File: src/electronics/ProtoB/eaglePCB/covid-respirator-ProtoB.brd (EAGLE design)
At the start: 160 x 100 mm, 18 parts, among them IC2 L7805CV-DG, Q1 VNP35N07-E, T2 BC548

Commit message: update protoB schematic
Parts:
- removed F1: 8A, fuse:19560
- removed Q1: VNP35N07-E, transistor-fet:TO220
- added IC1: (no value), analog-devices:SO8
- added IC3, IC4: AD8607R, analog-devices:SO8
- added LCD1: LCD_2X16_SIL, lcd_2x16_led_backlight:HY-1602F
- added LED1, LED3: ROUGE, led:LED3MM
- added LED2: VERTE, led:LED3MM
- added R10: 680, rcl:0207/10
- added R11: 10k, pot:SM-42/43B
- added R12: 68k, rcl:0207/10
- added R13: 33k, rcl:0207/10
- added R14: 22k, rcl:0207/10
- added R15: 12k, rcl:0207/10
- added R16, R17: 8.2k, rcl:0207/10
- added R18: 5.6k, rcl:0207/10
- added R19: 3.3k, rcl:0207/10
- added R20: 2.2k, rcl:0207/10
- added R21, R22, R26: 270, rcl:0207/10
- added R23, R24, R25: 10k, rcl:0207/10
- added R9: 150, rcl:0207/10
- added S1, S2, S3, S4, S5, S6, S7, S8: TL32YO, switch:TL3XYO
- C2: value 47uF/25v -> 10uF/25v
- C4: value 10uF -> 100nF
- R1, R4: value 100 -> 1.5k
- R2: value 3k -> 4k7
- R6: value 1k -> 12k
- R7: value 1k -> 1.5k
- R8: value 1k -> 150
- moved R4 137.2 mm to (-71.1, -88.9)
- moved R1 127.0 mm to (-71.1, -83.8)
- moved R8 95.7 mm to (-71.1, -133.3)
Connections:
- net A3 renamed A2
- removed net D6: R4.2
- new net +5VNUCLEO: IC3.4, LCD1.2, R1.1, R11.3, R16.1, R8.1
- new net 6546876: C4.1, IC1.3, R5.1
- new net A0: R12.2, R13.2, R14.2, R15.2, R16.2, R17.2, R18.2, R19.2, R20.2
- new net D10: LCD1.12
- new net D11: LCD1.13
- new net D12: LCD1.14
- new net D2: IC3.3, R24.1
- new net D4: IC3.5, R23.1
- new net D7: LCD1.4
- new net D8: LCD1.6
- new net D9: LCD1.11
- new net N$10: LCD1.3, R11.2
- new net N$11: R12.1, S8.1
- new net N$14: R13.1, S7.1
- new net N$15: R14.1, S6.1
- new net N$16: R15.1, S5.1
- new net N$18: R17.1, S4.1
- new net N$19: R18.1, S3.1
- new net N$20: R19.1, S2.1
- new net N$21: R20.1, S1.1
- new net N$22: LED3.K, R26.1
- new net N$23: LED1.K, R21.1
- new net N$24: LED2.K, R22.1
- new net N$26: LED3.A
- new net N$7: LCD1.15, R8.2
- new net N$8: IC1.2, IC1.6, R9.2
- new net PB13: LED2.A
- new net PC4: LED1.A
- new net V+: IC4.8
- new net V-: IC4.4
- net +12V: no longer F1.2
- net A1: now also R10.1, R9.1; no longer C4.1, R5.1
- net AGND: now also IC1.4, R10.2
- net AREF: now also IC1.7
- net D5: now also IC4.3, R25.1; no longer R1.2
- net GND: now also IC3.8, LCD1.1, LCD1.16, LCD1.5, R11.1, R21.2, R22.2, R23.2, R24.2, R25.2, R26.2, R4.2, S1.2, S2.2, S3.2, S4.2, S5.2, S6.2, S7.2, S8.2; no longer Q1.3, R8.1
- net N$1: now also IC4.1; no longer R1.1
- net N$4: now also IC3.2, IC3.6, IC4.2, R1.2, R4.1; no longer Q1.2
- net N$5: now also IC3.1; no longer F1.1
- net N$6: now also IC3.7; no longer Q1.1, R4.1, R8.2

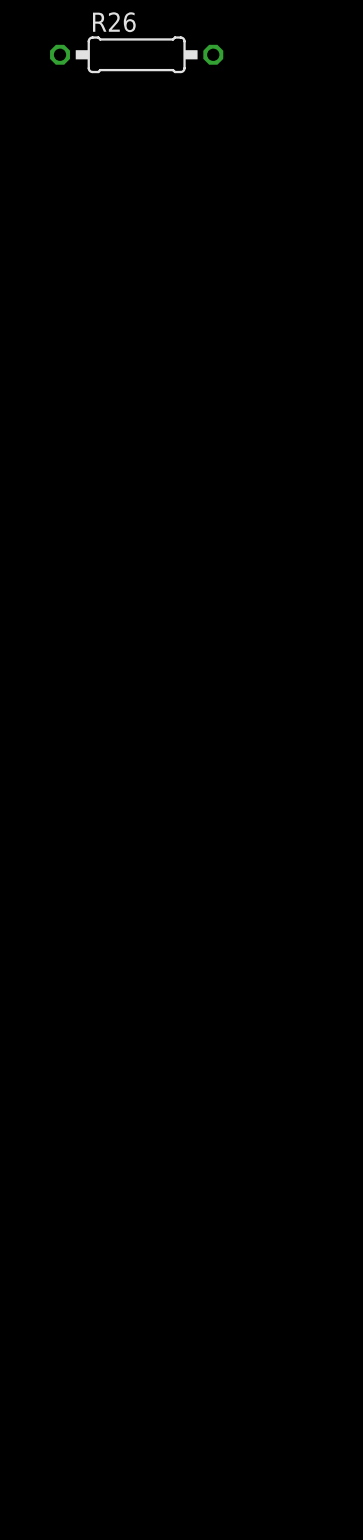
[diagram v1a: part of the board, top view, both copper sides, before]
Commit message: update protoB schematic
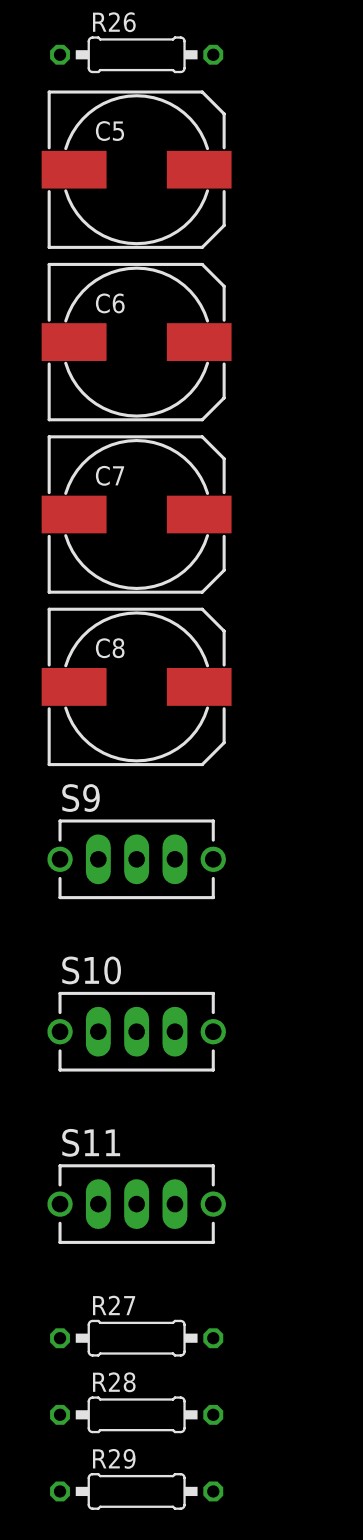
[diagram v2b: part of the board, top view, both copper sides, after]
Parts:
- added C5, C6: 47uF/6V, rcl:150CLZ-1010
- added C7, C8: 10uF, rcl:150CLZ-1010
- added R27, R28, R29: 10k, rcl:0207/10
- added S10, S11, S9: TL32YO, switch:TL3XYO
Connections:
- new net +3.3VNUCLEO: R16.1, S10.2, S11.2, S9.2
- new net +5V_S1: C5.+
- new net +5V_S2: C6.+
- new net PB1: R28.1, S10.1
- new net PB15: R27.1, S11.1
- new net PB2: R29.1, S9.1
- net +12V: now also C7.+, C8.+
- net +5VNUCLEO: no longer R16.1
- net GND: now also C5.-, C6.-, C7.-, C8.-, R27.2, R28.2, R29.2
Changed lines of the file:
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@@
 <element name="LED3" library="led" package="LED3MM" value="ROUGE" x="-82.55" y="-314.96"/>
 <element name="R26" library="rcl" package="0207/10" value="270" x="-78.74" y="-321.31"/>
+<element name="C5" library="rcl" package="150CLZ-1010" value="47uF/6V" x="-78.74" y="-328.93"/>
+<element name="C6" library="rcl" package="150CLZ-1010" value="47uF/6V" x="-78.74" y="-340.36"/>
+<element name="C7" library="rcl" package="150CLZ-1010" value="10uF" x="-78.74" y="-351.79"/>
+<element name="C8" library="rcl" package="150CLZ-1010" value="10uF" x="-78.74" y="-363.22"/>
+<element name="S9" library="switch" package="TL3XYO" value="TL32YO" x="-78.74" y="-374.65"/>
+<element name="S10" library="switch" package="TL3XYO" value="TL32YO" x="-78.74" y="-386.08"/>
+<element name="S11" library="switch" package="TL3XYO" value="TL32YO" x="-78.74" y="-397.51"/>
+<element name="R27" library="rcl" package="0207/10" value="10k" x="-78.74" y="-406.4"/>
+<element name="R28" library="rcl" package="0207/10" value="10k" x="-78.74" y="-411.48"/>
+<element name="R29" library="rcl" package="0207/10" value="10k" x="-78.74" y="-416.56"/>
 </elements>
 <signals>
@@
 <contactref element="R24" pad="2"/>
 <contactref element="R26" pad="2"/>
+<contactref element="C6" pad="-"/>
+<contactref element="C5" pad="-"/>
+<contactref element="C7" pad="-"/>
+<contactref element="C8" pad="-"/>
+<contactref element="R28" pad="2"/>
+<contactref element="R27" pad="2"/>
+<contactref element="R29" pad="2"/>
 <wire x1="-78.74" y1="-152.4" x2="-78.74" y2="-163.83" width="0" layer="19" extent="1-1"/>
 <wire x1="-78.74" y1="-140.97" x2="-78.74" y2="-152.4" width="0" layer="19" extent="1-1"/>
@@
 <wire x1="-73.66" y1="-311.15" x2="-73.66" y2="-306.07" width="0" layer="19" extent="1-1"/>
 <wire x1="-73.66" y1="-321.31" x2="-73.66" y2="-311.15" width="0" layer="19" extent="1-1"/>
+<wire x1="-82.89" y1="-328.93" x2="-73.66" y2="-321.31" width="0" layer="19" extent="1-1"/>
+<wire x1="-82.89" y1="-340.36" x2="-82.89" y2="-328.93" width="0" layer="19" extent="1-1"/>
+<wire x1="-82.89" y1="-351.79" x2="-82.89" y2="-340.36" width="0" layer="19" extent="1-1"/>
+<wire x1="-82.89" y1="-363.22" x2="-82.89" y2="-351.79" width="0" layer="19" extent="1-1"/>
+<wire x1="-73.66" y1="-406.4" x2="-82.89" y2="-363.22" width="0" layer="19" extent="1-1"/>
+<wire x1="-73.66" y1="-411.48" x2="-73.66" y2="-406.4" width="0" layer="19" extent="1-1"/>
+<wire x1="-73.66" y1="-416.56" x2="-73.66" y2="-411.48" width="0" layer="19" extent="1-1"/>
 <wire x1="-36.83" y1="45.72" x2="-62.23" y2="-20.32" width="0" layer="19" extent="1-1"/>
 </signal>
@@
 <contactref element="IC2" pad="1"/>
 <contactref element="SG1" pad="+"/>
+<contactref element="C7" pad="+"/>
+<contactref element="C8" pad="+"/>
+<wire x1="-74.59" y1="-351.79" x2="-74.59" y2="-363.22" width="0" layer="19" extent="1-1"/>
+<wire x1="-24.13" y1="-12.7" x2="-74.59" y2="-351.79" width="0" layer="19" extent="1-1"/>
 <wire x1="-35.56" y1="2.54" x2="-24.13" y2="-12.7" width="0" layer="19" extent="1-1"/>
 <wire x1="-26.33" y1="30.48" x2="-35.56" y2="2.54" width="0" layer="19" extent="1-1"/>
@@
 <contactref element="R8" pad="1"/>
 <contactref element="R11" pad="3"/>
-<contactref element="R16" pad="1"/>
 <wire x1="-79.95" y1="-130.69" x2="-76.2" y2="-133.35" width="0" layer="19" extent="1-1"/>
 <wire x1="-64.77" y1="-95.25" x2="-79.95" y2="-130.69" width="0" layer="19" extent="1-1"/>
 <wire x1="-76.2" y1="-83.82" x2="-64.77" y2="-95.25" width="0" layer="19" extent="1-1"/>
 <wire x1="-70.485" y1="-68.64" x2="-76.2" y2="-83.82" width="0" layer="19" extent="1-1"/>
-<wire x1="-83.82" y1="-275.59" x2="-76.2" y2="-133.35" width="0" layer="19" extent="1-1"/>
 </signal>
 <signal name="N$4">
@@
 <contactref element="LED3" pad="A"/>
 </signal>
+<signal name="+5V_S1">
+<contactref element="C5" pad="+"/>
+</signal>
+<signal name="+5V_S2">
+<contactref element="C6" pad="+"/>
+</signal>
+<signal name="PB15">
+<contactref element="R27" pad="1"/>
+<contactref element="S11" pad="1"/>
+<wire x1="-81.28" y1="-397.51" x2="-83.82" y2="-406.4" width="0" layer="19" extent="1-1"/>
+</signal>
+<signal name="PB1">
+<contactref element="R28" pad="1"/>
+<contactref element="S10" pad="1"/>
+<wire x1="-81.28" y1="-386.08" x2="-83.82" y2="-411.48" width="0" layer="19" extent="1-1"/>
+</signal>
+<signal name="PB2">
+<contactref element="R29" pad="1"/>
+<contactref element="S9" pad="1"/>
+<wire x1="-81.28" y1="-374.65" x2="-83.82" y2="-416.56" width="0" layer="19" extent="1-1"/>
+</signal>
+<signal name="+3.3VNUCLEO">
+<contactref element="R16" pad="1"/>
+<contactref element="S9" pad="2"/>
+<contactref element="S10" pad="2"/>
+<contactref element="S11" pad="2"/>
+<wire x1="-78.74" y1="-386.08" x2="-78.74" y2="-397.51" width="0" layer="19" extent="1-1"/>
+<wire x1="-78.74" y1="-374.65" x2="-78.74" y2="-386.08" width="0" layer="19" extent="1-1"/>
+<wire x1="-83.82" y1="-275.59" x2="-78.74" y2="-374.65" width="0" layer="19" extent="1-1"/>
+</signal>
 </signals>

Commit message: update protoB schematic
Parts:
- added C10, C11: 100nF, rcl:C050-050X075
- added C12: 47uF/6V, rcl:150CLZ-1010
- added C13: 10uF, rcl:150CLZ-1010
- added C9: 10uF/25v, rcl:150CLZ-1010
- added R30: 10k, rcl:0207/10
- added R31: 330, rcl:0207/10
- LED3: value ROUGE -> JAUNE
- R11: value 10k -> 9k1; device pot:SM-42/43B -> rcl:0207/10
- R7: value 1.5k -> 1.2k
- moved R11 346.7 mm to (-78.7, -476.2)
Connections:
- net N$26 renamed PB14
- removed net V+: IC4.8
- removed net V-: IC4.4
- new net D3: IC4.5, R30.1
- new net E5V: C9.+
- new net N$17: IC4.7
- net +12V: now also C10.1, C11.1, C13.+
- net +5VNUCLEO: now also IC4.8, R11.2; no longer R11.3
- net +5V_S2: now also C12.+
- net AGND: now also C11.2
- net GND: now also C10.2, C12.-, C13.-, C9.-, IC4.4, R30.2, R31.1; no longer R11.1
- net N$10: now also R11.1, R31.2; no longer R11.2
- net N$4: now also IC4.6

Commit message: schematic B5
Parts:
- added R32: 12k, rcl:0207/10
- added R33: 100R, rcl:0207/10
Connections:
- new net N$25: LCD1.14, R33.1
- new net PA13: LCD1.5, R32.2
- net D12: now also R33.2; no longer LCD1.14
- net GND: now also R32.1; no longer LCD1.5
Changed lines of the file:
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@@
 <element name="R11" library="rcl" package="0207/10" value="9k1" x="-78.74" y="-476.25"/>
 <element name="R31" library="rcl" package="0207/10" value="330" x="-78.74" y="-481.33"/>
+<element name="R32" library="rcl" package="0207/10" value="12k" x="-78.74" y="-486.41"/>
+<element name="R33" library="rcl" package="0207/10" value="100R" x="-78.74" y="-491.49"/>
 </elements>
 <signals>
@@
 <contactref element="LCD1" pad="16"/>
 <contactref element="LCD1" pad="1"/>
-<contactref element="LCD1" pad="5"/>
 <contactref element="S7" pad="2"/>
 <contactref element="S6" pad="2"/>
@@
 <contactref element="R30" pad="2"/>
 <contactref element="R31" pad="1"/>
+<contactref element="R32" pad="1"/>
 <wire x1="-78.74" y1="-434.34" x2="-82.89" y2="-424.18" width="0" layer="19" extent="1-1"/>
 <wire x1="-73.66" y1="-416.56" x2="-82.89" y2="-424.18" width="0" layer="19" extent="1-1"/>
@@
 <wire x1="-73.66" y1="-471.17" x2="-82.89" y2="-462.28" width="0" layer="19" extent="1-1"/>
 <wire x1="-83.82" y1="-481.33" x2="-73.66" y2="-471.17" width="0" layer="19" extent="1-1"/>
+<wire x1="-83.82" y1="-486.41" x2="-83.82" y2="-481.33" width="0" layer="19" extent="1-1"/>
 <wire x1="-82.89" y1="-363.22" x2="-73.66" y2="-406.4" width="0" layer="19" extent="1-1"/>
 <wire x1="-82.89" y1="-351.79" x2="-82.89" y2="-363.22" width="0" layer="19" extent="1-1"/>
@@
 <wire x1="-67.31" y1="-95.25" x2="-78.74" y2="-140.97" width="0" layer="19" extent="1-1"/>
 <wire x1="-66.04" y1="-88.9" x2="-67.31" y2="-95.25" width="0" layer="19" extent="1-1"/>
-<wire x1="-57.15" y1="-95.25" x2="-67.31" y2="-95.25" width="0" layer="19" extent="1-1"/>
 <wire x1="-70.485" y1="-78.8" x2="-66.04" y2="-88.9" width="0" layer="19" extent="1-1"/>
 <wire x1="-74.295" y1="-63.44" x2="-70.485" y2="-78.8" width="0" layer="19" extent="1-1"/>
-<wire x1="-29.21" y1="-95.25" x2="-57.15" y2="-95.25" width="0" layer="19" extent="1-1"/>
+<wire x1="-29.21" y1="-95.25" x2="-66.04" y2="-88.9" width="0" layer="19" extent="1-1"/>
 <wire x1="-57.15" y1="-27.94" x2="-74.295" y2="-63.44" width="0" layer="19" extent="1-1"/>
 <wire x1="-62.23" y1="-20.32" x2="-57.15" y2="-27.94" width="0" layer="19" extent="1-1"/>
@@
 </signal>
 <signal name="D12">
-<contactref element="LCD1" pad="14"/>
+<contactref element="R33" pad="2"/>
 </signal>
 <signal name="D11">
@@
 <contactref element="IC4" pad="7"/>
 </signal>
+<signal name="PA13">
+<contactref element="LCD1" pad="5"/>
+<contactref element="R32" pad="2"/>
+<wire x1="-73.66" y1="-486.41" x2="-57.15" y2="-95.25" width="0" layer="19" extent="1-1"/>
+</signal>
+<signal name="N$25">
+<contactref element="R33" pad="1"/>
+<contactref element="LCD1" pad="14"/>
+<wire x1="-83.82" y1="-491.49" x2="-34.29" y2="-95.25" width="0" layer="19" extent="1-1"/>
+</signal>
 </signals>
